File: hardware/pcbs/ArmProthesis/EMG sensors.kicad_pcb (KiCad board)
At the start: 4 copper layers, 65 x 26 mm, 30 parts, among them IC1 INA128, J2 Conn_01x01_Pin, J3 Conn_01x03_Pin, J4 Conn_01x01_Pin, U6 OPA2188AIDR, U7 OPA188AIDR

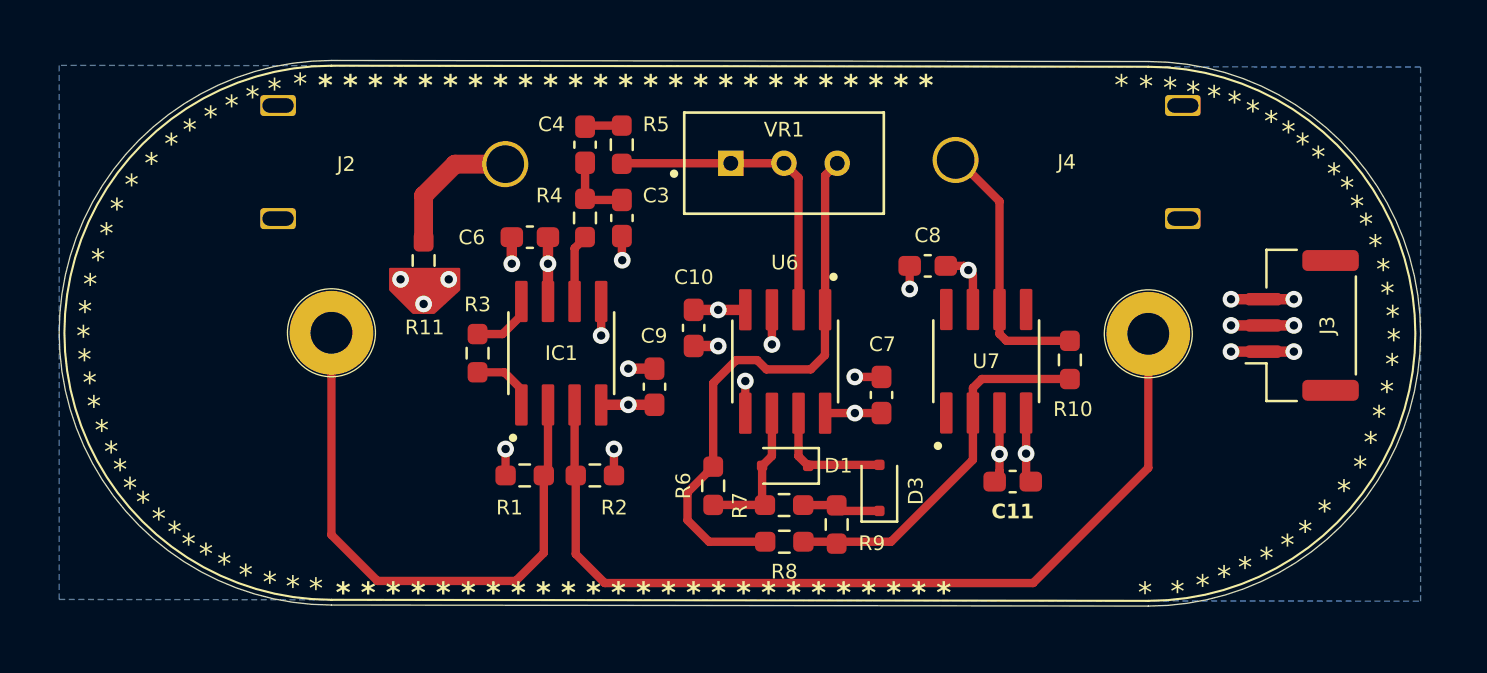
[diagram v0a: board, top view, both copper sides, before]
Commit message: sEMG critical  issue
Corrected inaccurate DIN 1.5mm jack footprint
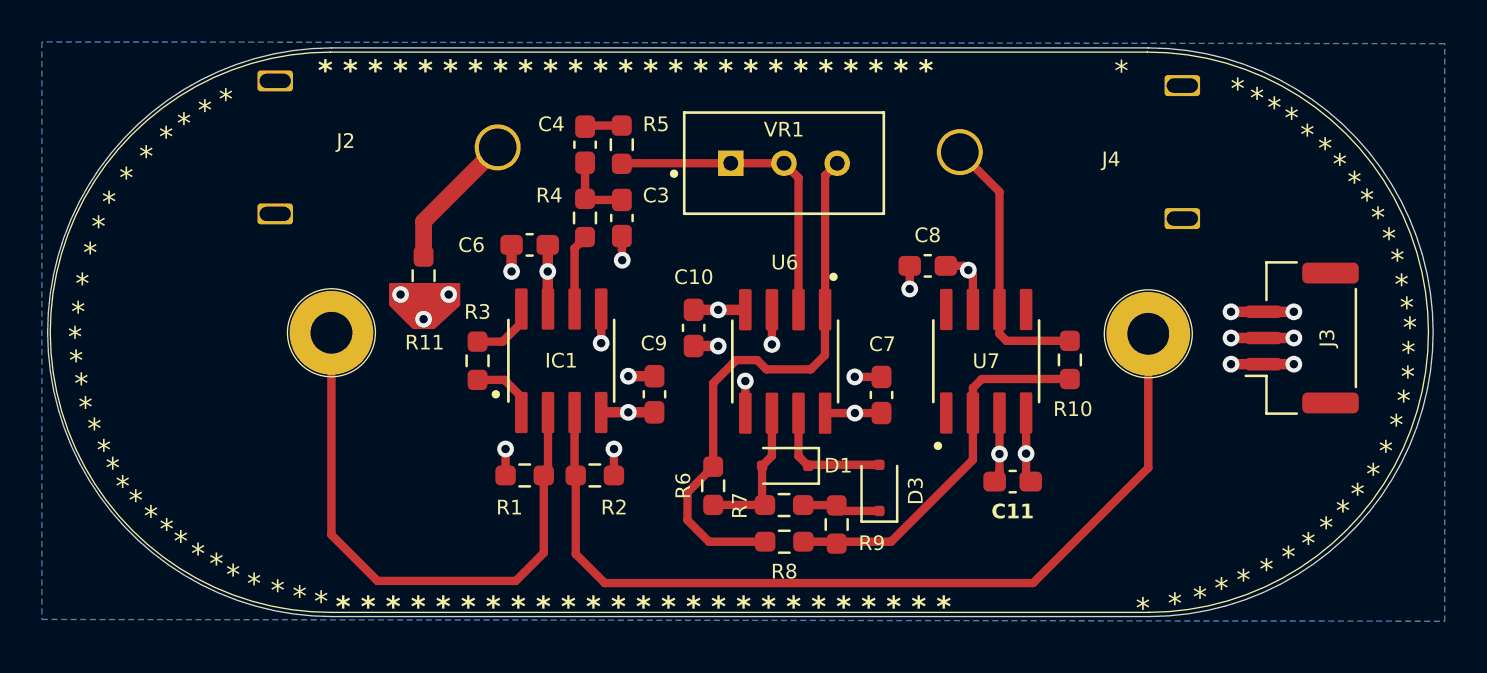
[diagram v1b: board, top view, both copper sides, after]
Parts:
- moved J2 3.14 mm to (112.7, 101.4)
- moved J4 2.65 mm to (149.2, 102.3)
- moved R11 0.73 mm to (116.4, 107.8)
- moved J3 0.60 mm to (158.3, 110.8)
- moved C6 0.37 mm to (121.5, 106.4)
- moved IC1 0.36 mm to (123.0, 111.9)
- moved R3 0.36 mm to (119.0, 111.9)
- moved C9 0.36 mm to (127.4, 113.5)
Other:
- board size 65 x 26 mm -> 66.2 x 27.1 mm

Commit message: .
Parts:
- removed C3: 8.2nF, Capacitor_SMD:C_0603_1608Metric_Pad1.08x0.95mm_HandSolder
- removed C4: 1uF, Capacitor_SMD:C_0603_1608Metric_Pad1.08x0.95mm_HandSolder
- removed U7: OPA188AIDR, OP AMPS:OPA188
- added C1: 250nF, Resistor_SMD:R_0402_1005Metric, F.Cu at (141.3, 106.0)
- added C2: 100nF, Resistor_SMD:R_0402_1005Metric, F.Cu at (143.4, 106.0)
- added R12: 10k, Resistor_SMD:R_0402_1005Metric, F.Cu at (125.8, 105.0)
- added U3: OPA2188AIDR, OP AMPS:OPA2188, F.Cu at (144.6, 111.7)
- R10, R3, R6, R7, R8, R9: footprint Resistor_SMD:R_0603_1608Metric_Pad0.98x0.95mm_HandSolder -> Resistor_SMD:R_0402_1005Metric
- R4: value 10k -> 33k; footprint Resistor_SMD:R_0603_1608Metric_Pad0.98x0.95mm_HandSolder -> Resistor_SMD:R_0402_1005Metric
- R5: value 10k -> 3.16k; footprint Resistor_SMD:R_0603_1608Metric_Pad0.98x0.95mm_HandSolder -> Resistor_SMD:R_0402_1005Metric
- U6: footprint OP AMPS:ОПА2188AIDR -> OP AMPS:OPA2188
- moved R5 18.4 mm to (143.4, 107.2), turned to 0 degrees
- moved R4 16.1 mm to (139.4, 109.9)
- moved C8 9.81 mm to (148.3, 113.3), turned to 90 degrees
- moved C11 8.50 mm to (140.8, 110.0), turned to -90 degrees
- moved R10 5.13 mm to (144.6, 116.2), turned to 0 degrees
- moved VR1 2.67 mm to (132.8, 105.0)
- moved U2 0.46 mm to (151.5, 110.5)
- moved U6 0.08 mm to (133.7, 112.0)
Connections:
- R10 pad 2: /AEMG -> non-filtered
- R4 pad 1: Net-(IC1-Pad6) -> non-filtered
- R4 pad 2: Net-(C3-Pad1) -> Net-(C1-Pad2)
- R5 pad 1: Net-(U6--INA) -> Net-(C1-Pad2)
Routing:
- net non-filtered: track 0.00 -> 10.7 mm
- net Net-(C1-Pad2): track 0.00 -> 7.36 mm
- net Net-(U3--INB): track 18.0 -> 13.8 mm
- net Net-(U6--INA): track 15.2 -> 11.6 mm
- net Net-(C3-Pad1): track 3.52 -> 0.00 mm
- net /AEMG: track 13.0 -> 9.74 mm
- net INVERTED: track 26.8 -> 24.1 mm
- net /+5.5V: track 12.7 -> 10.5 mm
- net /-5.5V: track 11.4 -> 9.89 mm
- net Net-(IC1-Pad6): track 3.65 -> 5.11 mm
- net GND: track 21.3 -> 20.6 mm, vias 17 -> 18

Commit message: updates
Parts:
- removed C2: 100nF, Resistor_SMD:R_0402_1005Metric
- added C3: 100nF, Resistor_SMD:R_0402_1005Metric, F.Cu at (147.2, 110.8)
- C1: value 250nF -> 100nF
- R10: value 20k -> 10kΩ
- R4: value 33k -> 6.8kΩ
- R5: value 3.16k -> 75kΩ
- R8: value 20k -> 6.8k
- R9: value 10k -> 10.5kΩ
- moved R8 18.0 mm to (147.2, 108.7), turned to -90 degrees
- moved R9 14.5 mm to (144.9, 108.2), turned to 0 degrees
- moved R10 9.36 mm to (143.8, 106.9)
- moved R4 8.89 mm to (148.3, 110.8)
- moved C1 2.31 mm to (142.6, 107.9)
- moved R5 1.96 mm to (142.6, 109.0)
- moved C11 1.88 mm to (140.0, 111.7)
- moved U3 1.88 mm to (143.8, 113.4)
- moved C8 1.88 mm to (147.5, 115.0)
- moved R6 1.28 mm to (130.5, 119.1)
- moved R7 1.03 mm to (133.1, 119.6)
- moved D3 0.59 mm to (138.1, 118.5)
- moved VR1 0.59 mm to (132.8, 105.6)
- moved C6 0.59 mm to (121.4, 106.9)
- moved C9 0.59 mm to (127.4, 114.1)
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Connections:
- C1 pad 2: Net-(C1-Pad2) -> Net-(U3-+INA)
- R10 pad 1: Net-(U3--INB) -> GND
- R10 pad 2: non-filtered -> FB
- R4 pad 2: Net-(C1-Pad2) -> Net-(C3-Pad2)
- R5 pad 1: Net-(C1-Pad2) -> GND
- R8 pad 1: Net-(U3--INB) -> /AEMG
- R8 pad 2: INVERTED -> Net-(C3-Pad2)
- R9 pad 1: Net-(D3-K) -> FB
- R9 pad 2: Net-(U3--INB) -> /AEMG
- U3 pad 2: /AEMG -> FB
- U3 pad 5: GND -> Net-(D3-K)
- U3 pad 6: Net-(U3--INB) -> non-filtered
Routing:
- net Net-(U3--INB): track 13.8 -> 0.00 mm
- net Net-(C1-Pad2): track 7.36 -> 0.00 mm
- net Net-(U3-+INA): track 1.97 -> 9.14 mm
- net Net-(D3-K): track 4.27 -> 10.9 mm
- net INVERTED: track 24.1 -> 17.9 mm
- net FB: track 0.00 -> 4.27 mm
- net non-filtered: track 10.7 -> 7.23 mm
- net Net-(C3-Pad2): track 0.00 -> 2.21 mm
- net Vin2: track 41.5 -> 43.2 mm
- net /AEMG: track 9.74 -> 8.31 mm
- net Vin1: track 26.3 -> 25.7 mm
- net Net-(IC1-Pad8): track 2.76 -> 3.34 mm
- net Net-(IC1-Pad1): track 3.18 -> 3.72 mm
- net Net-(D1-A): track 7.49 -> 6.94 mm
- net GND: track 20.6 -> 20.9 mm, vias 18 -> 19

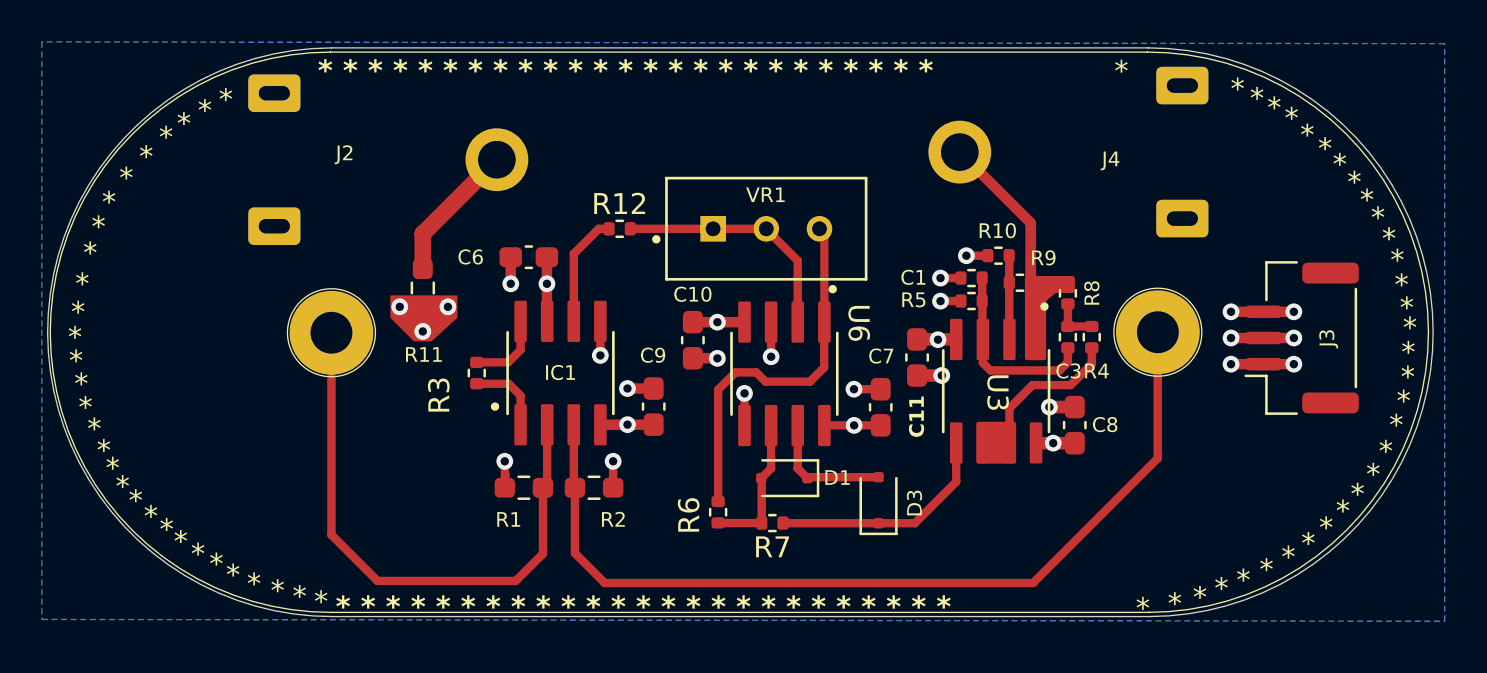
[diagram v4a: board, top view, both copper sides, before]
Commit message: Fixed compatibility of connectors  + new BMS chip
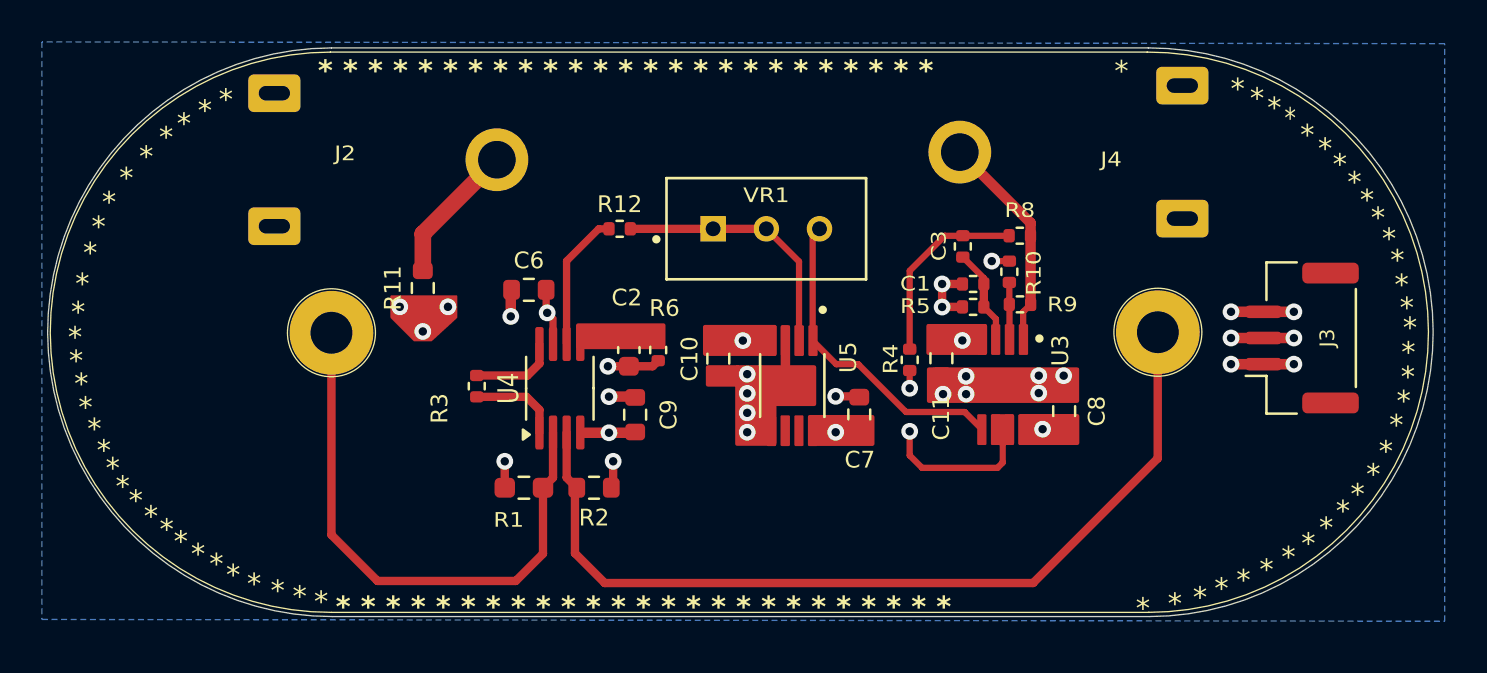
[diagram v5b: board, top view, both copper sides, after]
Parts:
- removed D1, D3: BAT54J, Diode_SMD:D_SOD-323F
- removed IC1: INA128, OP AMPS:INA128U
- removed R7: 20k, Resistor_SMD:R_0402_1005Metric
- removed U6: OPA2188AIDR, OP AMPS:OPA2188
- added C2: -, Capacitor_SMD:C_0603_1608Metric, F.Cu at (126.2, 111.4)
- added U4: INA326, Package_SO:MSOP-8_3x3mm_P0.65mm, F.Cu at (122.9, 113.2)
- added U5: LME49726MY, OP AMPS:LME49726MY, F.Cu at (134.0, 113.1)
- C1: value 100nF -> 7.87uF
- C10, C11, C6, C7, C8, C9: footprint Capacitor_SMD:C_0603_1608Metric_Pad1.08x0.95mm_HandSolder -> Resistor_SMD:R_0603_1608Metric
- C3: value 100nF -> 316nF
- R10: value 10kΩ -> 1k
- R11, R2: footprint Resistor_SMD:R_0603_1608Metric_Pad0.98x0.95mm_HandSolder -> Resistor_SMD:R_0603_1608Metric
- R3: value 200 -> 2k
- R4: value 6.8kΩ -> 1k
- R5: value 75kΩ -> 1k
- R6: value 20k -> 249k
- R8: value 6.8k -> 1k
- R9: value 10.5kΩ -> 10k
- U3: value OPA2188AIDR -> LME49726MY; footprint OP AMPS:OPA2188 -> OP AMPS:LME49726MY
- moved R4 8.76 mm to (139.6, 111.8)
- moved R6 8.25 mm to (127.6, 111.4), turned to 90 degrees
- moved C3 6.63 mm to (142.1, 106.4)
- moved R8 3.58 mm to (144.9, 105.9), turned to 180 degrees
- moved C6 1.56 mm to (121.4, 108.5)
- moved C10 1.50 mm to (130.5, 111.8)
- moved C11 1.16 mm to (141.1, 111.8)
- moved C7 1.08 mm to (137.2, 114.5)
- moved R9 1.03 mm to (144.9, 109.2)
- moved C9 0.97 mm to (126.5, 114.5)
- moved R10 0.93 mm to (144.4, 107.6), turned to -90 degrees
- moved C8 0.84 mm to (147.0, 114.3)
- moved R3 0.62 mm to (118.9, 113.1)
- moved U3 0.46 mm to (144.1, 113.0)
- moved C1 0.29 mm to (142.6, 108.2)
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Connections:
- C10 pad 1: /-5.5V -> /-2.5V
- C11 pad 1: /-5.5V -> /-2.5V
- C6 pad 1: /+5.5V -> /+2.5V
- C7 pad 1: /+5.5V -> /+2.5V
- C8 pad 1: /+5.5V -> /+2.5V
- C9 pad 1: /-5.5V -> /-2.5V
- J3 pad 1: /+5.5V -> /-2.5V
- J3 pad 2: /-5.5V -> GND
- J3 pad 3: GND -> /+2.5V
- R11 pad 1: GND -> /+2.5V
- R2 pad 1: Vin2 -> GND
- R2 pad 2: GND -> Vin2
- R6 pad 1: INVERTED -> GND
- U3 pad 4: /-5.5V -> /-2.5V
- U3 pad 5: Net-(D3-K) -> INVERTED
- U3 pad 8: /+5.5V -> /+2.5V
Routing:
- net Net-(D3-K): track 10.9 -> 0.00 mm
- net /+5.5V: track 10.5 -> 0.00 mm, vias 5 -> 0
- net /-5.5V: track 9.89 -> 0.00 mm, vias 5 -> 0
- net /-2.5V: track 0.00 -> 7.92 mm, vias 0 -> 5
- net Net-(U4-R2): track 6.94 -> 0.00 mm
- net Net-(C3-Pad2): track 2.21 -> 9.11 mm
- net Net-(D1-K): track 6.13 -> 0.00 mm
- net /+2.5V: track 0.00 -> 5.33 mm, vias 0 -> 8
- net GND: track 20.9 -> 15.6 mm, vias 19 -> 21
- net Net-(U3-POSA): track 9.14 -> 4.50 mm
- net non-filtered: track 7.23 -> 10.6 mm, vias 0 -> 2
- net INVERTED: track 17.9 -> 15.2 mm
- net /AEMG: track 8.31 -> 10.5 mm
- net FB: track 4.27 -> 2.71 mm
- net Net-(R12-Pad1): track 5.40 -> 6.62 mm
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- added copper zone on In2.Cu, net /+2.5V
- added copper zone on B.Cu, net /-2.5V
- removed copper zone on In2.Cu, net /+5.5V
- removed copper zone on B.Cu, net /-5.5V

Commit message: Ordered versions
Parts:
- removed J4: Conn_01x01_Pin, Connectors:DIN_Male_1PIN_1.5mm
- added J1: Conn_01x02_Pin, Connector_JST:JST_GH_SM02B-GHS-TB_1x02-1MP_P1.25mm_Horizontal, F.Cu at (146.9, 100.3)
- C1: value 7.87uF -> 10uF; footprint Resistor_SMD:R_0402_1005Metric -> Capacitor_SMD:C_0402_1005Metric
- C10, C11, C6, C7, C8, C9: footprint Resistor_SMD:R_0603_1608Metric -> Capacitor_SMD:C_0603_1608Metric
- C2: value - -> DNP
- C3: value 316nF -> 330nF; footprint Resistor_SMD:R_0402_1005Metric -> Capacitor_SMD:C_0402_1005Metric
- J2: value Conn_01x01_Pin -> DNP
- VR1: footprint Trimmers:TRIM_3296W-1-104ALF -> Potentiometer_THT:Potentiometer_Bourns_3296W_Vertical
- moved C1 2.81 mm to (142.6, 111.0)
- moved C11 2.81 mm to (141.1, 114.6)
- moved C3 2.81 mm to (142.1, 109.2)
- moved R4 2.81 mm to (139.6, 114.7)
- moved R5 2.81 mm to (142.6, 112.1)
- moved R8 2.81 mm to (144.9, 108.7)
- moved R9 2.81 mm to (144.9, 112.0)
- moved C8 2.81 mm to (147.0, 117.1)
- moved R10 2.81 mm to (144.4, 110.4)
- moved U3 2.81 mm to (144.1, 115.8)
- moved VR1 2.54 mm to (130.2, 105.6), turned to 180 degrees
- moved J3 2.38 mm to (160.7, 110.7)
- moved J2 1.52 mm to (114.1, 102.4)
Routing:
- net INVERTED: track 15.2 -> 18.0 mm
- net /AEMG: track 10.5 -> 12.3 mm
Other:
- board text added: "* * * * * * * * * * * * * * * * * * * * *"
